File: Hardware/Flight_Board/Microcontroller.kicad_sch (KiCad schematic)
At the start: 20 parts, among them J3 Conn_01x04, J4 Conn_01x06, SW1 SW_Push, U1 FT5HN

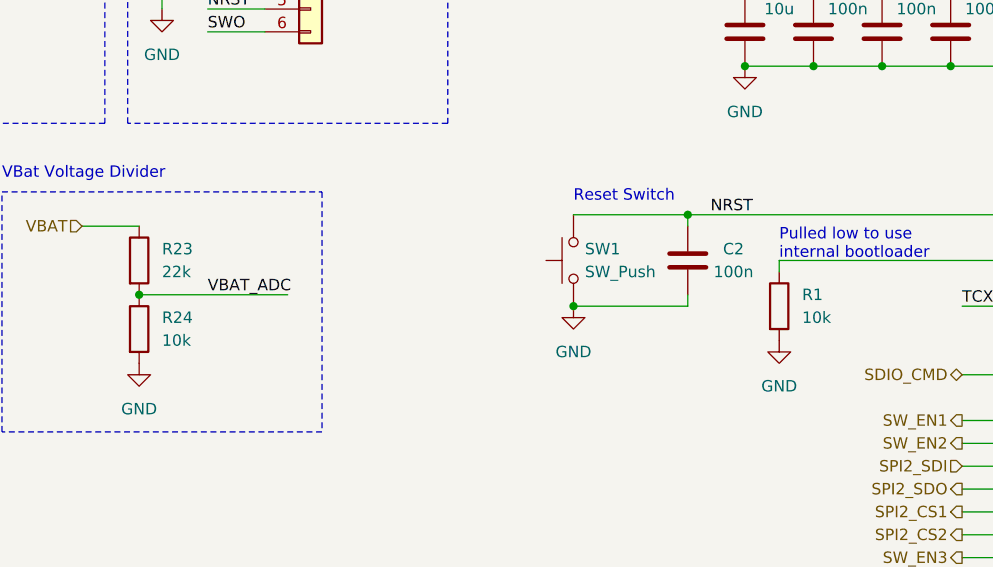
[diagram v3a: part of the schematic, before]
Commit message: Clean up, relabel all refdes, and add autosaved files to gitignore
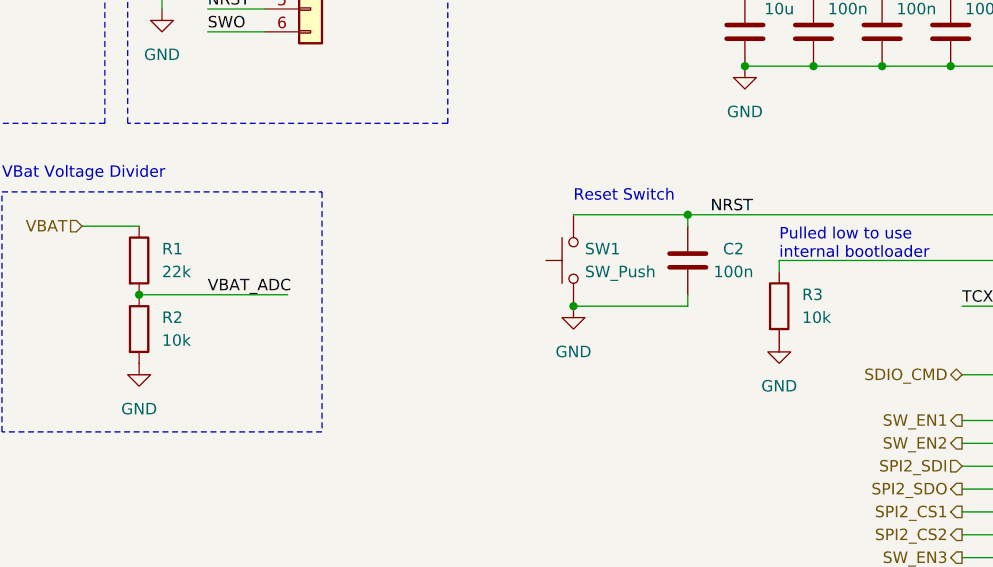
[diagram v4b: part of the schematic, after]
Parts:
- renumbered R23 to R1, R24 to R2, R1 to R3
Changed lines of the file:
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@@
   (symbol (lib_id "Device:R") (at 146.05 68.58 0) (unit 1)
     (in_bom yes) (on_board yes) (dnp no) (fields_autoplaced)
-    (property "Reference" "R1" (at 148.59 67.31 0)
+    (property "Reference" "R3" (at 148.59 67.31 0)
       (effects (font (size 1.27 1.27)) (justify left))
     )
@@
       (project "Flight_Board"
         (path "/e8eb85d5-f1ff-4500-895d-25b9ff5f6d36/fd3d6b0b-6f33-4db6-8189-55f0522596d3"
-          (reference "R1") (unit 1)
+          (reference "R3") (unit 1)
         )
       )
@@
   (symbol (lib_id "power:GND") (at 166.37 135.89 0) (unit 1)
     (in_bom yes) (on_board yes) (dnp no)
-    (property "Reference" "#PWR014" (at 166.37 142.24 0)
+    (property "Reference" "#PWR015" (at 166.37 142.24 0)
       (effects (font (size 1.27 1.27)) hide)
     )
@@
       (project "Flight_Board"
         (path "/e8eb85d5-f1ff-4500-895d-25b9ff5f6d36/fd3d6b0b-6f33-4db6-8189-55f0522596d3"
-          (reference "#PWR014") (unit 1)
+          (reference "#PWR015") (unit 1)
         )
       )
@@
   (symbol (lib_id "power:GND") (at 123.19 68.58 0) (unit 1)
     (in_bom yes) (on_board yes) (dnp no) (fields_autoplaced)
-    (property "Reference" "#PWR010" (at 123.19 74.93 0)
+    (property "Reference" "#PWR011" (at 123.19 74.93 0)
       (effects (font (size 1.27 1.27)) hide)
     )
@@
       (project "Flight_Board"
         (path "/e8eb85d5-f1ff-4500-895d-25b9ff5f6d36/fd3d6b0b-6f33-4db6-8189-55f0522596d3"
-          (reference "#PWR010") (unit 1)
+          (reference "#PWR011") (unit 1)
         )
       )
@@
   (symbol (lib_id "power:GND") (at 194.31 149.86 0) (unit 1)
     (in_bom yes) (on_board yes) (dnp no) (fields_autoplaced)
-    (property "Reference" "#PWR016" (at 194.31 156.21 0)
+    (property "Reference" "#PWR017" (at 194.31 156.21 0)
       (effects (font (size 1.27 1.27)) hide)
     )
@@
       (project "Flight_Board"
         (path "/e8eb85d5-f1ff-4500-895d-25b9ff5f6d36/fd3d6b0b-6f33-4db6-8189-55f0522596d3"
-          (reference "#PWR016") (unit 1)
+          (reference "#PWR017") (unit 1)
         )
       )
@@
   (symbol (lib_id "Device:R") (at 74.93 63.5 0) (unit 1)
     (in_bom yes) (on_board yes) (dnp no) (fields_autoplaced)
-    (property "Reference" "R23" (at 77.47 62.23 0)
+    (property "Reference" "R1" (at 77.47 62.23 0)
       (effects (font (size 1.27 1.27)) (justify left))
     )
@@
       (project "Flight_Board"
         (path "/e8eb85d5-f1ff-4500-895d-25b9ff5f6d36/fd3d6b0b-6f33-4db6-8189-55f0522596d3"
-          (reference "R23") (unit 1)
+          (reference "R1") (unit 1)
         )
       )
@@
   (symbol (lib_id "power:GND") (at 142.24 41.91 0) (unit 1)
     (in_bom yes) (on_board yes) (dnp no) (fields_autoplaced)
-    (property "Reference" "#PWR012" (at 142.24 48.26 0)
+    (property "Reference" "#PWR013" (at 142.24 48.26 0)
       (effects (font (size 1.27 1.27)) hide)
     )
@@
       (project "Flight_Board"
         (path "/e8eb85d5-f1ff-4500-895d-25b9ff5f6d36/fd3d6b0b-6f33-4db6-8189-55f0522596d3"
-          (reference "#PWR012") (unit 1)
+          (reference "#PWR013") (unit 1)
         )
       )
@@
   (symbol (lib_id "Device:R") (at 74.93 71.12 0) (unit 1)
     (in_bom yes) (on_board yes) (dnp no) (fields_autoplaced)
-    (property "Reference" "R24" (at 77.47 69.85 0)
+    (property "Reference" "R2" (at 77.47 69.85 0)
       (effects (font (size 1.27 1.27)) (justify left))
     )
@@
       (project "Flight_Board"
         (path "/e8eb85d5-f1ff-4500-895d-25b9ff5f6d36/fd3d6b0b-6f33-4db6-8189-55f0522596d3"
-          (reference "R24") (unit 1)
+          (reference "R2") (unit 1)
         )
       )
@@
   (symbol (lib_id "power:GND") (at 146.05 72.39 0) (unit 1)
     (in_bom yes) (on_board yes) (dnp no) (fields_autoplaced)
-    (property "Reference" "#PWR013" (at 146.05 78.74 0)
+    (property "Reference" "#PWR014" (at 146.05 78.74 0)
       (effects (font (size 1.27 1.27)) hide)
     )
@@
       (project "Flight_Board"
         (path "/e8eb85d5-f1ff-4500-895d-25b9ff5f6d36/fd3d6b0b-6f33-4db6-8189-55f0522596d3"
-          (reference "#PWR013") (unit 1)
+          (reference "#PWR014") (unit 1)
         )
       )
@@
   (symbol (lib_id "power:+3.3V") (at 77.47 25.4 0) (unit 1)
     (in_bom yes) (on_board yes) (dnp no)
-    (property "Reference" "#PWR08" (at 77.47 29.21 0)
+    (property "Reference" "#PWR09" (at 77.47 29.21 0)
       (effects (font (size 1.27 1.27)) hide)
     )
@@
       (project "Flight_Board"
         (path "/e8eb85d5-f1ff-4500-895d-25b9ff5f6d36/fd3d6b0b-6f33-4db6-8189-55f0522596d3"
-          (reference "#PWR08") (unit 1)
+          (reference "#PWR09") (unit 1)
         )
       )
@@
   (symbol (lib_id "power:GND") (at 217.17 45.72 0) (unit 1)
     (in_bom yes) (on_board yes) (dnp no) (fields_autoplaced)
-    (property "Reference" "#PWR018" (at 217.17 52.07 0)
+    (property "Reference" "#PWR019" (at 217.17 52.07 0)
       (effects (font (size 1.27 1.27)) hide)
     )
@@
       (project "Flight_Board"
         (path "/e8eb85d5-f1ff-4500-895d-25b9ff5f6d36/fd3d6b0b-6f33-4db6-8189-55f0522596d3"
+          (reference "#PWR019") (unit 1)
+        )
+      )
+    )
+  )
+  (symbol (lib_id "power:+3.3V") (at 201.93 30.48 0) (unit 1)
+    (in_bom yes) (on_board yes) (dnp no) (fields_autoplaced)
+    (property "Reference" "#PWR018" (at 201.93 34.29 0)
+      (effects (font (size 1.27 1.27)) hide)
+    )
+    (property "Value" "+3.3V" (at 201.93 25.4 0)
+      (effects (font (size 1.27 1.27)))
+    )
+    (property "Footprint" "" (at 201.93 30.48 0)
+      (effects (font (size 1.27 1.27)) hide)
+    )
+    (property "Datasheet" "" (at 201.93 30.48 0)
+      (effects (font (size 1.27 1.27)) hide)
+    )
+    (pin "1")
+    (instances
+      (project "Flight_Board"
+        (path "/e8eb85d5-f1ff-4500-895d-25b9ff5f6d36/fd3d6b0b-6f33-4db6-8189-55f0522596d3"
           (reference "#PWR018") (unit 1)
         )
@@
     )
   )
-  (symbol (lib_id "power:+3.3V") (at 201.93 30.48 0) (unit 1)
-    (in_bom yes) (on_board yes) (dnp no) (fields_autoplaced)
-    (property "Reference" "#PWR017" (at 201.93 34.29 0)
-      (effects (font (size 1.27 1.27)) hide)
-    )
-    (property "Value" "+3.3V" (at 201.93 25.4 0)
-      (effects (font (size 1.27 1.27)))
-    )
-    (property "Footprint" "" (at 201.93 30.48 0)
-      (effects (font (size 1.27 1.27)) hide)
-    )
-    (property "Datasheet" "" (at 201.93 30.48 0)
-      (effects (font (size 1.27 1.27)) hide)
-    )
-    (pin "1")
-    (instances
-      (project "Flight_Board"
-        (path "/e8eb85d5-f1ff-4500-895d-25b9ff5f6d36/fd3d6b0b-6f33-4db6-8189-55f0522596d3"
-          (reference "#PWR017") (unit 1)
-        )
-      )
-    )
-  )
   (symbol (lib_id "Device:C") (at 157.48 38.1 0) (unit 1)
     (in_bom yes) (on_board yes) (dnp no)
@@
   (symbol (lib_id "power:+3.3V") (at 142.24 30.48 0) (unit 1)
     (in_bom yes) (on_board yes) (dnp no) (fields_autoplaced)
-    (property "Reference" "#PWR011" (at 142.24 34.29 0)
+    (property "Reference" "#PWR012" (at 142.24 34.29 0)
       (effects (font (size 1.27 1.27)) hide)
     )
@@
       (project "Flight_Board"
         (path "/e8eb85d5-f1ff-4500-895d-25b9ff5f6d36/fd3d6b0b-6f33-4db6-8189-55f0522596d3"
-          (reference "#PWR011") (unit 1)
+          (reference "#PWR012") (unit 1)
         )
       )
@@
   (symbol (lib_id "power:GND") (at 74.93 74.93 0) (unit 1)
     (in_bom yes) (on_board yes) (dnp no) (fields_autoplaced)
-    (property "Reference" "#PWR060" (at 74.93 81.28 0)
+    (property "Reference" "#PWR08" (at 74.93 81.28 0)
       (effects (font (size 1.27 1.27)) hide)
     )
@@
       (project "Flight_Board"
         (path "/e8eb85d5-f1ff-4500-895d-25b9ff5f6d36/fd3d6b0b-6f33-4db6-8189-55f0522596d3"
-          (reference "#PWR060") (unit 1)
+          (reference "#PWR08") (unit 1)
         )
       )
@@
   (symbol (lib_id "power:+3.3V") (at 189.23 48.26 0) (unit 1)
     (in_bom yes) (on_board yes) (dnp no) (fields_autoplaced)
-    (property "Reference" "#PWR015" (at 189.23 52.07 0)
+    (property "Reference" "#PWR016" (at 189.23 52.07 0)
       (effects (font (size 1.27 1.27)) hide)
     )
@@
       (project "Flight_Board"
         (path "/e8eb85d5-f1ff-4500-895d-25b9ff5f6d36/fd3d6b0b-6f33-4db6-8189-55f0522596d3"
-          (reference "#PWR015") (unit 1)
+          (reference "#PWR016") (unit 1)
         )
       )
@@
   (symbol (lib_id "power:GND") (at 77.47 35.56 0) (unit 1)
     (in_bom yes) (on_board yes) (dnp no) (fields_autoplaced)
-    (property "Reference" "#PWR09" (at 77.47 41.91 0)
+    (property "Reference" "#PWR010" (at 77.47 41.91 0)
       (effects (font (size 1.27 1.27)) hide)
     )
@@
       (project "Flight_Board"
         (path "/e8eb85d5-f1ff-4500-895d-25b9ff5f6d36/fd3d6b0b-6f33-4db6-8189-55f0522596d3"
-          (reference "#PWR09") (unit 1)
-        )
-      )
+          (reference "#PWR010") (unit 1)
+        )
+      )

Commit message: clean up, implement suggestions from saunders
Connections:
- net +3.3V: no longer U1.3 (OUT), U?.5 (PH0)
- net ACCEL_INT: now reaches U?.41 (PA8)
- net IMU_INT: now reaches U?.44 (PA11)
- net BARO_INT: now reaches U?.45 (PA12)
- new net TCXO_OUT: U1.3 (OUT), U?.5 (PH0)
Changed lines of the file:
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@@
   (junction (at 142.24 30.48) (diameter 0) (color 0 0 0 0)
   )
-  (junction (at 57.15 25.4) (diameter 0) (color 0 0 0 0)
-  )
   (junction (at 172.72 30.48) (diameter 0) (color 0 0 0 0)
   )
@@
   )
   (junction (at 123.19 68.58) (diameter 0) (color 0 0 0 0)
-  )
-  (junction (at 43.18 25.4) (diameter 0) (color 0 0 0 0)
   )
   (junction (at 26.67 25.4) (diameter 0) (color 0 0 0 0)
@@
     (stroke (width 0) (type default))
   )
+  (wire (pts (xy 212.09 86.36) (xy 220.98 86.36))
+    (stroke (width 0) (type default))
+  )
   (wire (pts (xy 194.31 149.86) (xy 194.31 147.32))
     (stroke (width 0) (type default))
@@
     (stroke (width 0) (type default))
   )
-  (wire (pts (xy 57.15 25.4) (xy 66.04 25.4))
-    (stroke (width 0) (type default))
-  )
   (wire (pts (xy 166.37 81.28) (xy 176.53 81.28))
     (stroke (width 0) (type default))
@@
     (stroke (width 0) (type default))
   )
-  (wire (pts (xy 43.18 25.4) (xy 57.15 25.4))
-    (stroke (width 0) (type default))
-  )
   (wire (pts (xy 212.09 93.98) (xy 220.98 93.98))
     (stroke (width 0) (type default))
@@
     (stroke (width 0) (type default))
   )
+  (wire (pts (xy 212.09 78.74) (xy 220.98 78.74))
+    (stroke (width 0) (type default))
+  )
   (wire (pts (xy 166.37 93.98) (xy 176.53 93.98))
     (stroke (width 0) (type default))
@@
     (stroke (width 0) (type default))
   )
-  (wire (pts (xy 57.15 33.02) (xy 57.15 25.4))
-    (stroke (width 0) (type default))
-  )
   (wire (pts (xy 123.19 58.42) (xy 135.89 58.42))
     (stroke (width 0) (type default))
@@
     (stroke (width 0) (type default))
   )
-  (wire (pts (xy 50.8 33.02) (xy 57.15 33.02))
+  (wire (pts (xy 50.8 33.02) (xy 66.04 33.02))
     (stroke (width 0) (type default))
   )
@@
   )
   (wire (pts (xy 165.1 30.48) (xy 165.1 34.29))
+    (stroke (width 0) (type default))
+  )
+  (wire (pts (xy 212.09 88.9) (xy 220.98 88.9))
     (stroke (width 0) (type default))
   )
@@
     (effects (font (size 1.27 1.27)) (justify left bottom))
   )
-  (label "TCXO_OUT" (at 57.15 25.4 0) (fields_autoplaced)
+  (label "TCXO_OUT" (at 57.15 33.02 0) (fields_autoplaced)
     (effects (font (size 1.27 1.27)) (justify left bottom))
   )
@@
     (effects (font (size 1.27 1.27)) (justify left))
   )
+  (hierarchical_label "ACCEL_INT" (shape input) (at 220.98 78.74 0) (fields_autoplaced)
+    (effects (font (size 1.27 1.27)) (justify left))
+  )
   (hierarchical_label "SDIO_D2" (shape bidirectional) (at 166.37 106.68 180) (fields_autoplaced)
     (effects (font (size 1.27 1.27)) (justify right))
@@
     (effects (font (size 1.27 1.27)) (justify right))
   )
+  (hierarchical_label "IMU_INT" (shape input) (at 220.98 86.36 0) (fields_autoplaced)
+    (effects (font (size 1.27 1.27)) (justify left))
+  )
+  (hierarchical_label "BARO_INT" (shape input) (at 220.98 88.9 0) (fields_autoplaced)
+    (effects (font (size 1.27 1.27)) (justify left))
+  )
   (hierarchical_label "SDIO_CLK" (shape output) (at 220.98 137.16 0) (fields_autoplaced)
